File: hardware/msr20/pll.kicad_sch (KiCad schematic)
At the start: 9 parts, among them U6 74LS163, U7 CD74HC4046

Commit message: assign footprints for active components
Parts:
- U6, U7: footprint (none) -> Package_DIP:DIP-16_W7.62mm_LongPads
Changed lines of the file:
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@@
 			)
 		)
-		(property "Footprint" ""
+		(property "Footprint" "Package_DIP:DIP-16_W7.62mm_LongPads"
 			(at 165.1 71.12 0)
 			(effects
@@
 			)
 		)
-		(property "Footprint" ""
+		(property "Footprint" "Package_DIP:DIP-16_W7.62mm_LongPads"
 			(at 101.6 72.39 0)
 			(effects

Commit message: update footprint assignments for passives
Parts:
- C5, C6, C7, C8, C9: footprint (none) -> Capacitor_SMD:C_0805_2012Metric
- R2, R3: footprint (none) -> Resistor_SMD:R_0805_2012Metric
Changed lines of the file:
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@@
 			)
 		)
-		(property "Footprint" ""
+		(property "Footprint" "Resistor_SMD:R_0805_2012Metric"
 			(at 116.332 105.41 90)
 			(effects
@@
 			)
 		)
-		(property "Footprint" ""
+		(property "Footprint" "Capacitor_SMD:C_0805_2012Metric"
 			(at 79.0448 86.36 0)
 			(effects
@@
 			)
 		)
-		(property "Footprint" ""
+		(property "Footprint" "Resistor_SMD:R_0805_2012Metric"
 			(at 69.85 112.268 90)
 			(effects
@@
 			)
 		)
-		(property "Footprint" ""
+		(property "Footprint" "Capacitor_SMD:C_0805_2012Metric"
 			(at 73.66 95.5548 0)
 			(effects
@@
 			)
 		)
-		(property "Footprint" ""
+		(property "Footprint" "Capacitor_SMD:C_0805_2012Metric"
 			(at 84.1248 125.73 0)
 			(effects
@@
 			)
 		)
-		(property "Footprint" ""
+		(property "Footprint" "Capacitor_SMD:C_0805_2012Metric"
 			(at 132.08 75.2348 0)
 			(effects
@@
 			)
 		)
-		(property "Footprint" ""
+		(property "Footprint" "Capacitor_SMD:C_0805_2012Metric"
 			(at 82.55 77.7748 0)
 			(effects

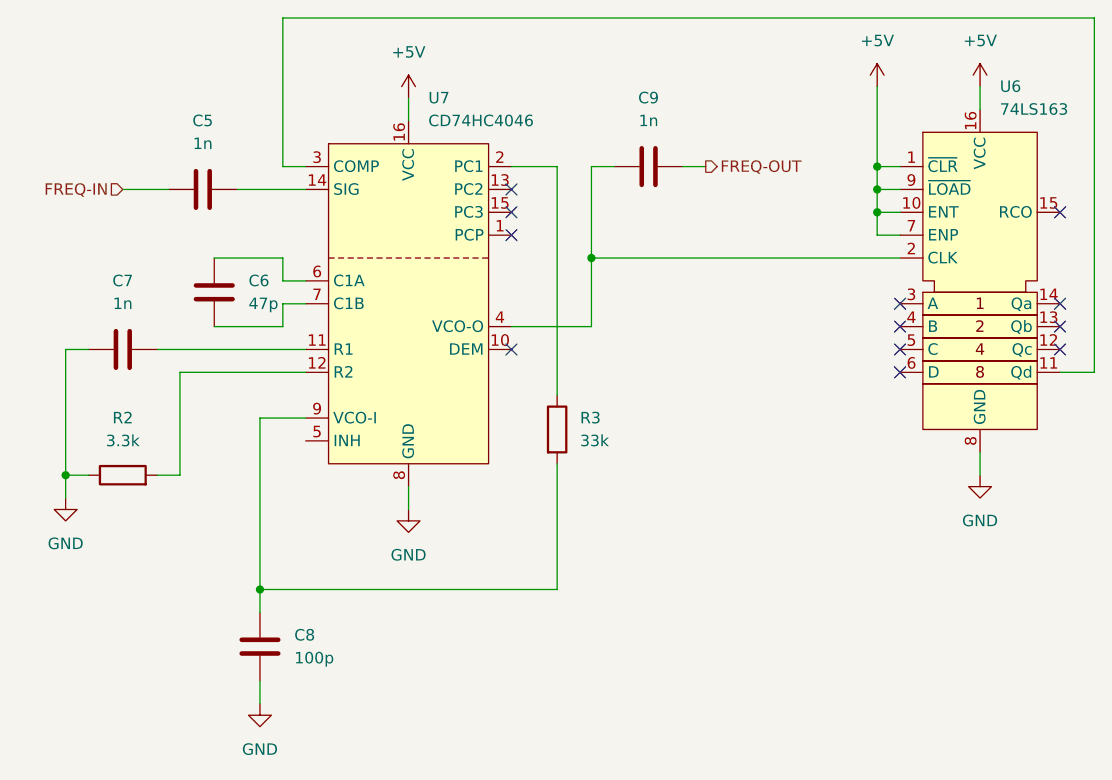
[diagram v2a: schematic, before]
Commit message: rf-bpf, lna, pll, rf mixer added to pcb
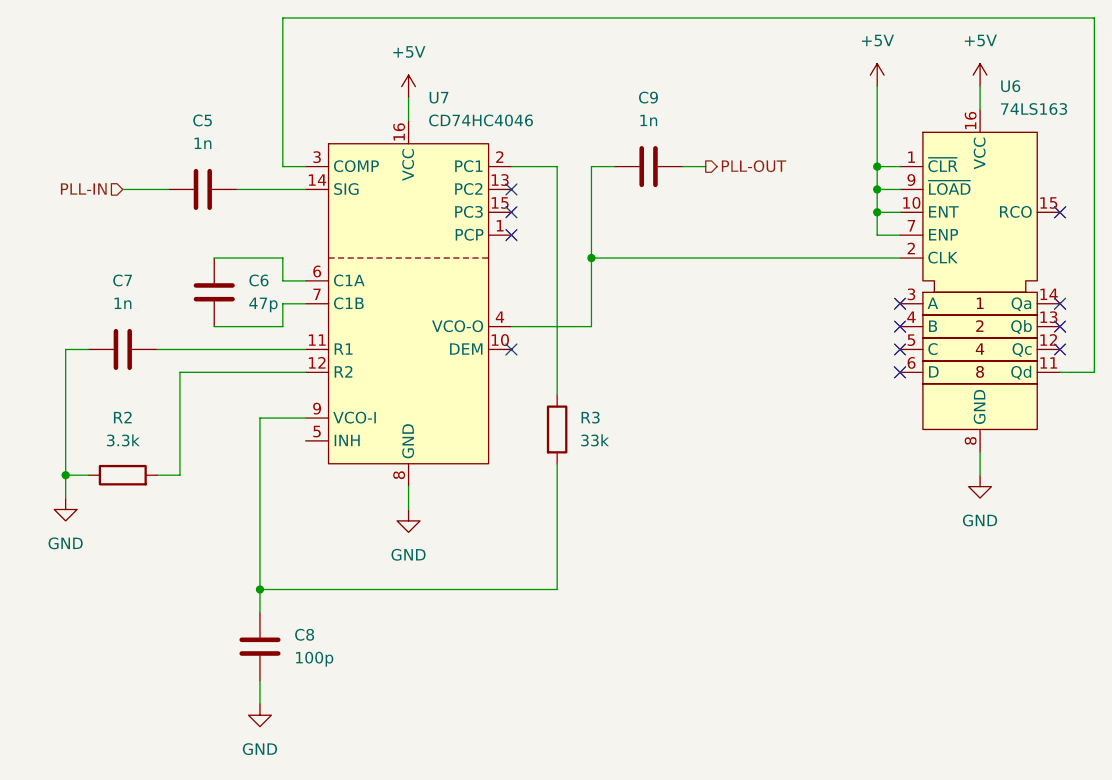
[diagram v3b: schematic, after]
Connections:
- net FREQ-IN renamed PLL-IN
- net FREQ-OUT renamed PLL-OUT
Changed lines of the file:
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@@
 		)
 	)
-	(hierarchical_label "FREQ-OUT"
+	(hierarchical_label "PLL-OUT"
 		(shape output)
 		(at 134.62 76.2 0)
@@
 		)
 	)
-	(hierarchical_label "FREQ-IN"
+	(hierarchical_label "PLL-IN"
 		(shape input)
 		(at 69.85 78.74 180)
